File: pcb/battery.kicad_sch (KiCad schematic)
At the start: 38 parts

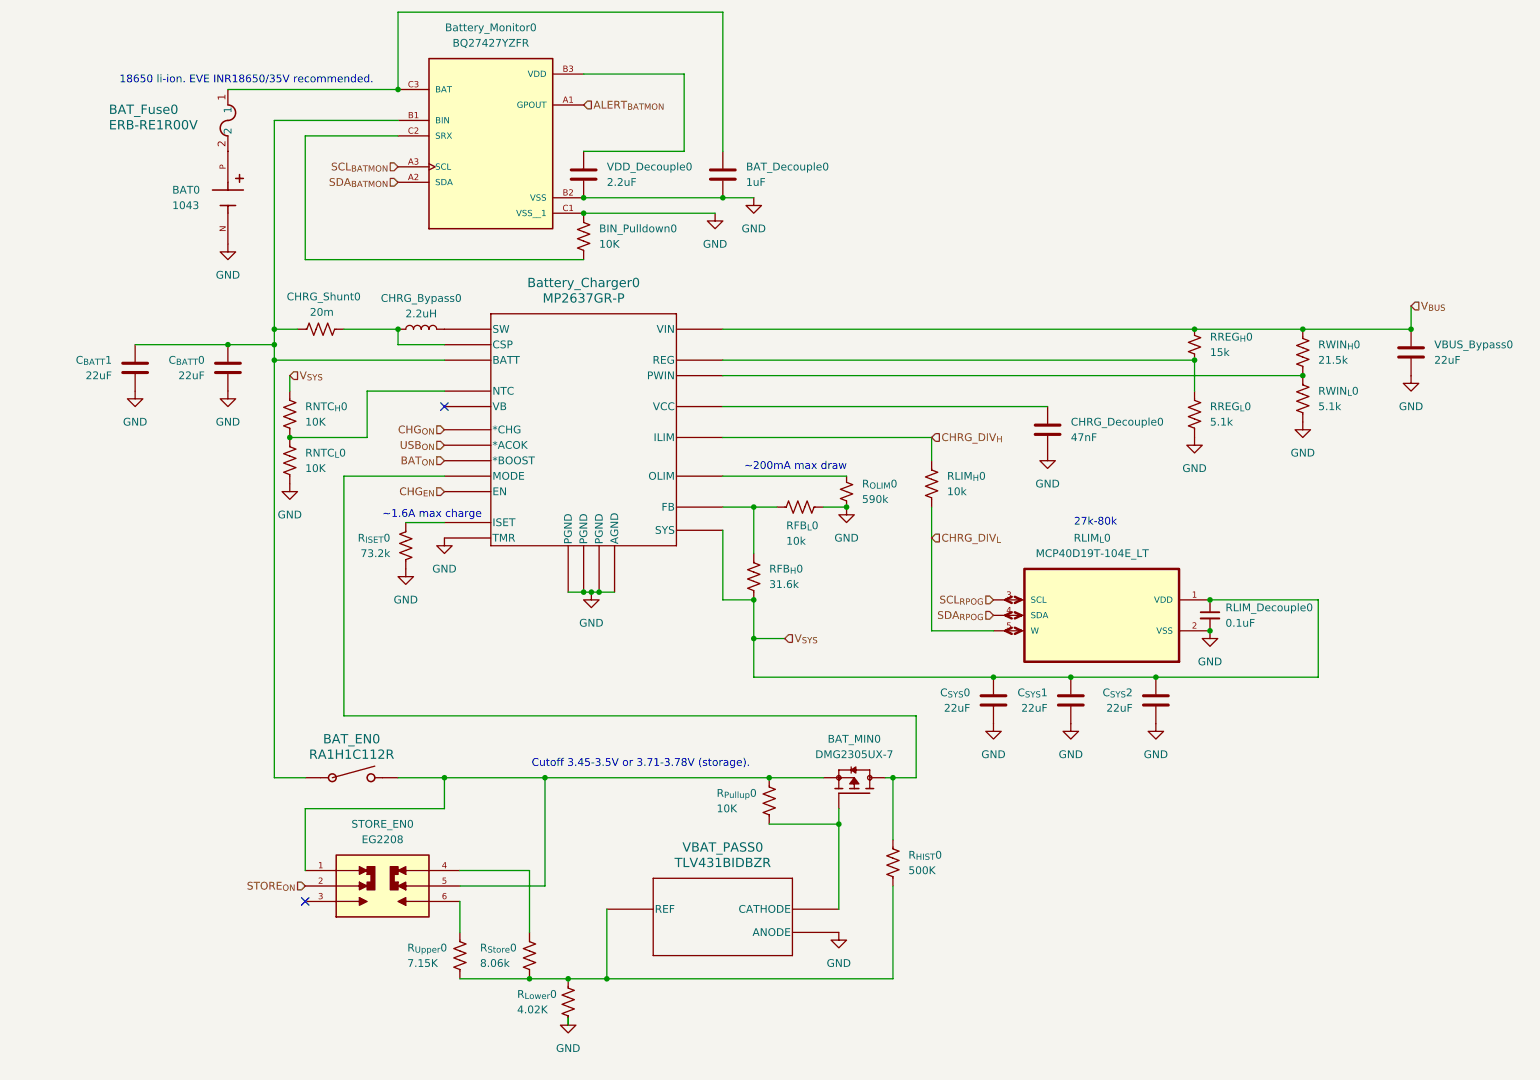
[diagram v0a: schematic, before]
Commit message: Label parts for JLCPCB
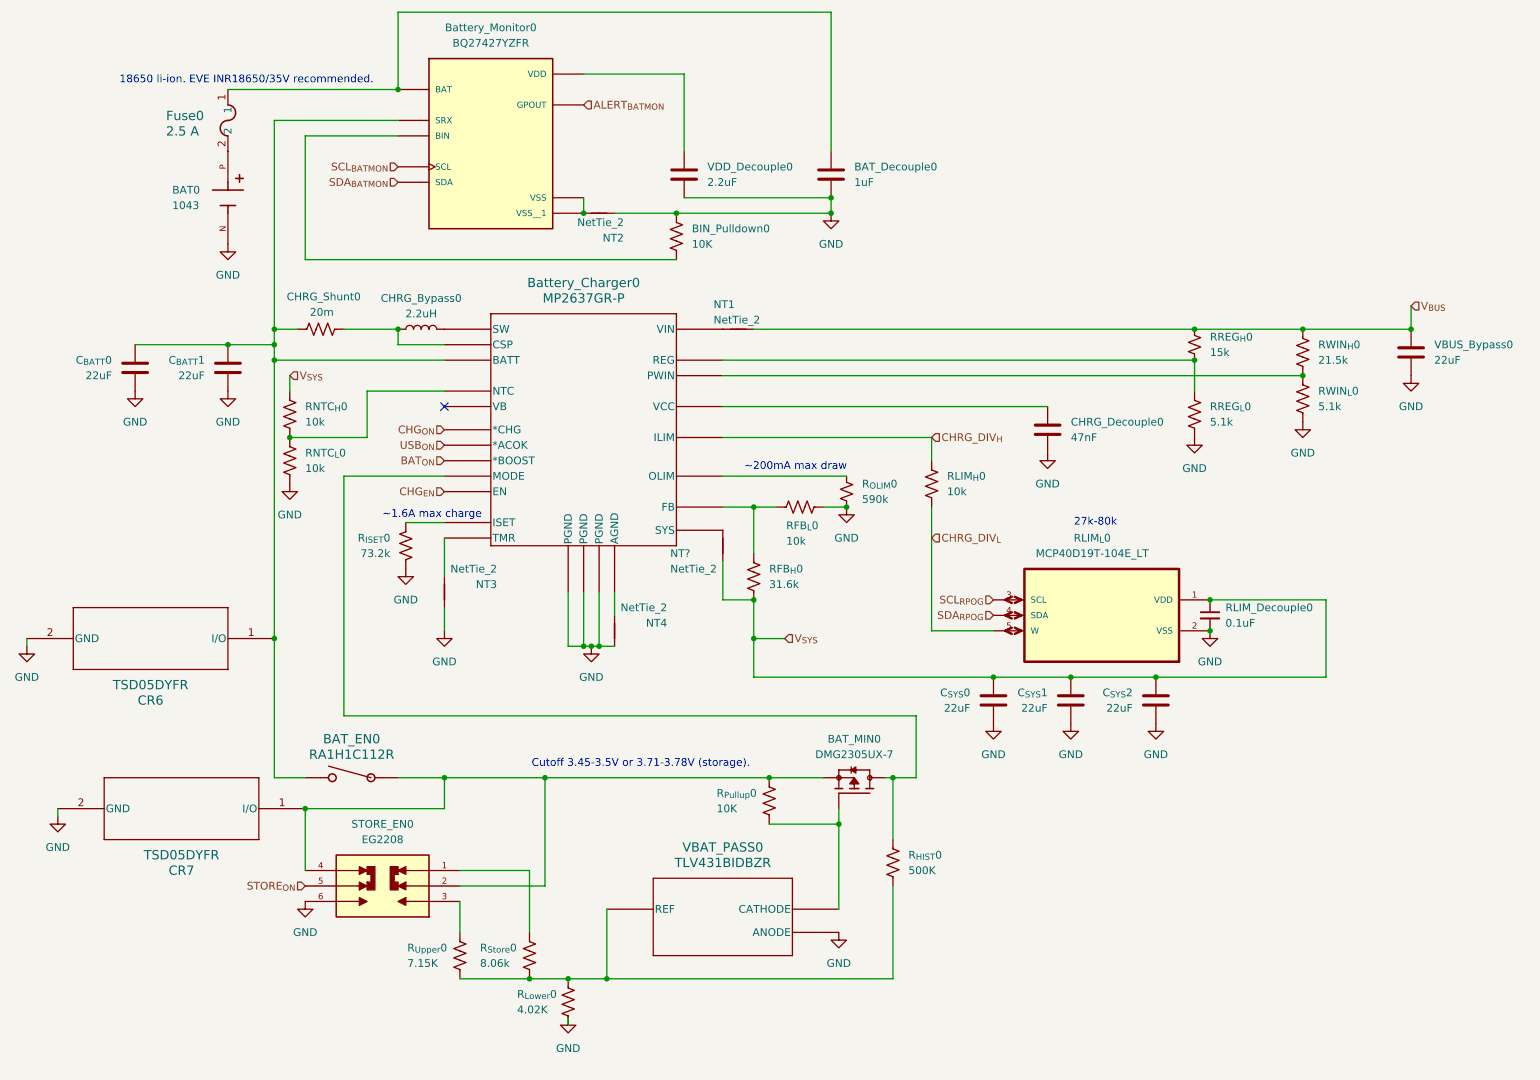
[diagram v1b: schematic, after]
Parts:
- added CR6, CR7: TSD05DYFR, TVS_SOD2_DYF_TEX, symbol TSD05DYFR:TSD05DYFR
- added NT1, NT2, NT3, NT4, NT?: NetTie_2, NetTie:NetTie-2_SMD_Pad0.5mm, symbol Device:NetTie_2
- BAT0: footprint 1043:BAT_1043 -> BAT_1043; symbol 1043:1043 -> 1042:1042; MAXIMUM_PACKAGE_HEIGHT 14.86mm -> 15.11mm; PARTREV J -> E; SNAPEDA_PN 1043 -> 1042
- BAT_MIN0: LCSC (none) -> C150470
- Battery_Charger0: LCSC (none) -> C97258
- Battery_Monitor0: footprint BQ27427YZFR:IC_BQ27427YZFR -> IC_BQ27427YZFR; LCSC (none) -> C6075475
- Fuse0: renamed from BAT_Fuse0; value ERB-RE1R00V -> 2.5 A; LCSC (none) -> C3166421
- RLIM_{L}0: LCSC (none) -> C623424
- RNTC_{H}0, RNTC_{L}0: value 10K -> 10k
- VBAT_PASS0: LCSC (none) -> C398375
- renumbered C_{BATT}1 to C_{BATT}0, C_{BATT}0 to C_{BATT}1
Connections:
- net GND: now also STORE_EN0.6, CR6.2 (GND), CR7.2 (GND), NT2.1, NT3.2, NT4.2; no longer Battery_Charger0.13 (TMR), Battery_Charger0.6 (AGND), Battery_Monitor0.B2 (VSS), Battery_Monitor0.C1 (VSS__1)
- net STORE_{ON}: now also STORE_EN0.5; no longer STORE_EN0.2
- net V_{BUS}: now also NT1.2; no longer Battery_Charger0.20 (VIN)
- net V_{SYS}: now also NT?.1; no longer Battery_Charger0.21 (SYS)
- net at Battery_Charger0.5 (BATT), CHRG_Shunt0.1, C_{BATT}0.1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: now also BAT_EN0.2, Battery_Monitor0.C2 (SRX), CR6.1 (I/O); no longer BAT_EN0.1, Battery_Monitor0.B1 (BIN)
- net at BIN_Pulldown0.2: now also Battery_Monitor0.B1 (BIN); no longer Battery_Monitor0.C2 (SRX)
- net at R_{Upper}0.1: now also STORE_EN0.3; no longer STORE_EN0.6
- net at STORE_EN0.4: now also BAT_EN0.1, BAT_MIN0.2, R_{Pullup}0.1, STORE_EN0.2, CR7.1 (I/O); no longer R_{Store}0.1
- new net: Battery_Monitor0.B2 (VSS), Battery_Monitor0.C1 (VSS__1), NT2.2
- new net: Battery_Charger0.21 (SYS), NT?.2
- new net: Battery_Charger0.13 (TMR), NT3.1
- new net: Battery_Charger0.20 (VIN), NT1.1
- new net: Battery_Charger0.6 (AGND), NT4.1
- new net: R_{Store}0.1, STORE_EN0.1
- no-connect marks 2 -> 1
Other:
- moved on the sheet: BAT_Decouple0, BIN_Pulldown0, VDD_Decouple0

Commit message: Add DNP for right hand
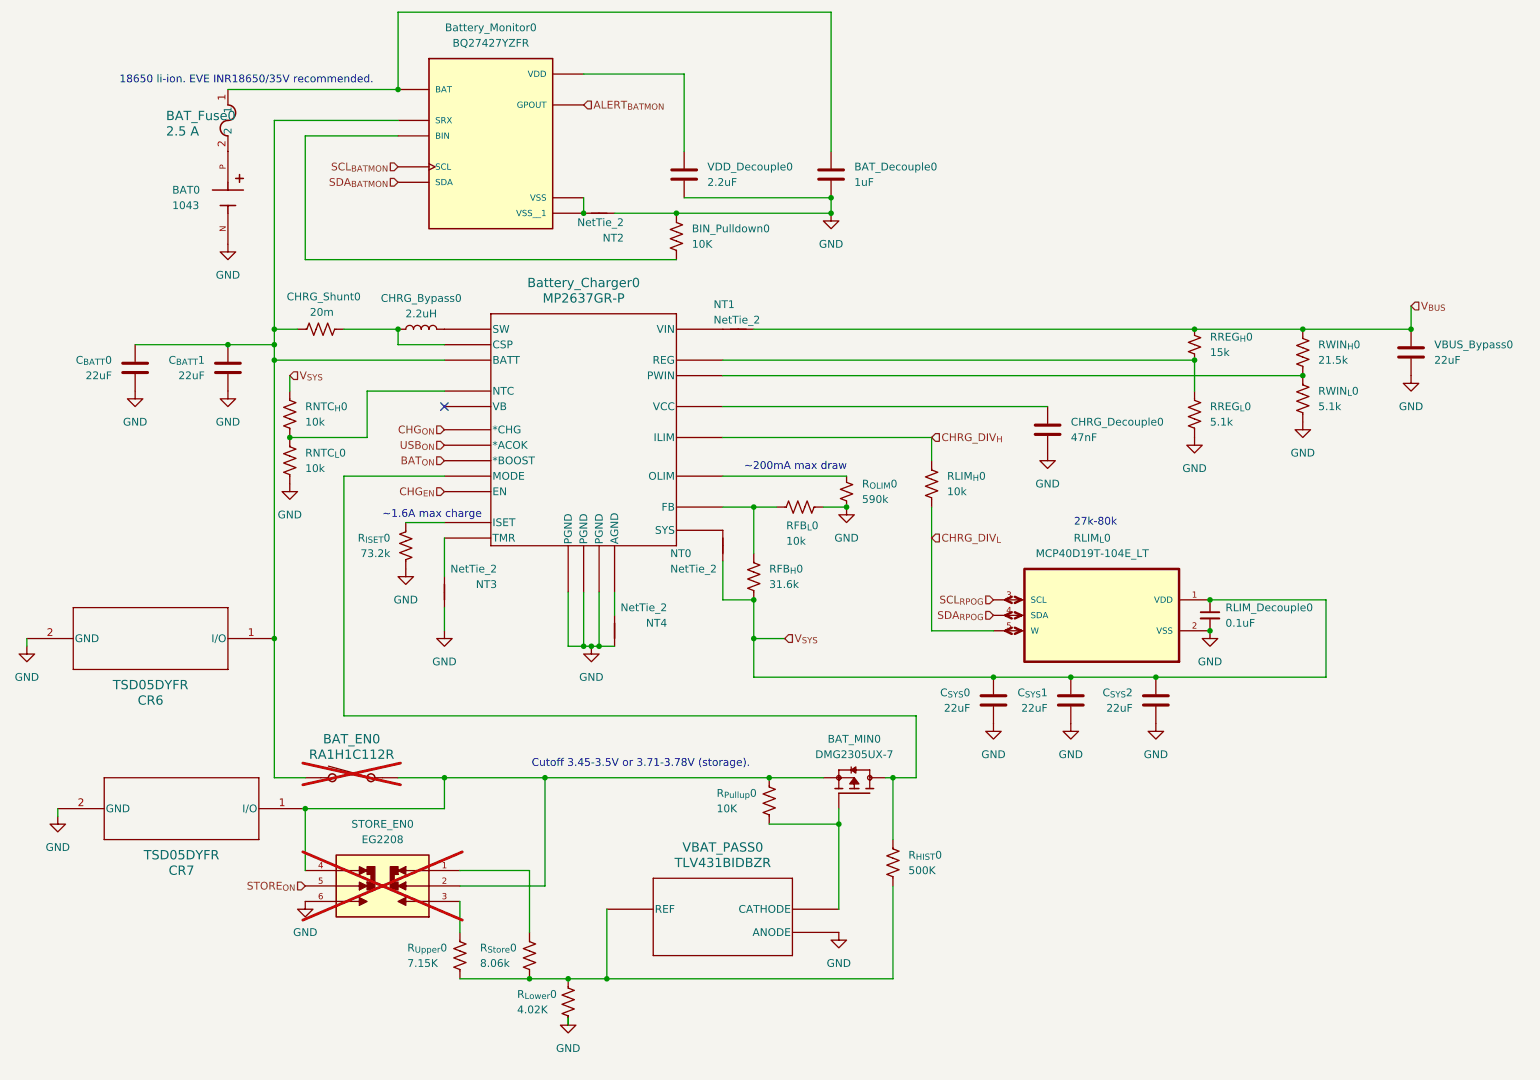
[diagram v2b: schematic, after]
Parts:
- BAT_EN0, STORE_EN0: now not fitted
- gave numbers to parts that had none: 1
- renumbered Fuse0 to BAT_Fuse0
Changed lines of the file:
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@@
 		(dnp no)
 		(fields_autoplaced yes)
-		(property "Reference" "#PWR030"
+		(property "Reference" "#PWR012"
 			(at 181.61 147.32 0)
 			(effects
@@
 		(dnp no)
 		(fields_autoplaced yes)
-		(property "Reference" "#PWR021"
+		(property "Reference" "#PWR04"
 			(at 85.09 121.92 0)
 			(effects
@@
 		(dnp no)
 		(fields_autoplaced yes)
-		(property "Reference" "#PWR013"
+		(property "Reference" "#PWR011"
 			(at 157.48 111.76 0)
 			(effects
@@
 		(dnp no)
 		(fields_autoplaced yes)
-		(property "Reference" "#PWR024"
+		(property "Reference" "#PWR018"
 			(at 232.41 97.79 0)
 			(effects
@@
 		(in_bom yes)
 		(on_board yes)
-		(dnp no)
+		(dnp yes)
 		(property "Reference" "BAT_EN0"
 			(at 76.2 143.51 0)
@@
 		(dnp no)
 		(fields_autoplaced yes)
-		(property "Reference" "#PWR027"
+		(property "Reference" "#PWR00"
 			(at 40.64 92.71 0)
 			(effects
@@
 		(on_board yes)
 		(dnp no)
-		(property "Reference" "NT?"
+		(property "Reference" "NT0"
 			(at 128.524 113.03 90)
 			(effects
@@
 		(dnp no)
 		(fields_autoplaced yes)
-		(property "Reference" "#PWR018"
+		(property "Reference" "#PWR08"
 			(at 154.94 63.5 0)
 			(effects
@@
 		(dnp no)
 		(fields_autoplaced yes)
-		(property "Reference" "#PWR012"
+		(property "Reference" "#PWR016"
 			(at 214.63 100.33 0)
 			(effects
@@
 		(dnp no)
 		(fields_autoplaced yes)
-		(property "Reference" "#PWR023"
+		(property "Reference" "#PWR017"
 			(at 217.17 132.08 0)
 			(effects
@@
 		(on_board yes)
 		(dnp no)
-		(property "Reference" "#PWR025"
+		(property "Reference" "#PWR07"
 			(at 115.57 134.62 0)
 			(effects
@@
 		(dnp no)
 		(fields_autoplaced yes)
-		(property "Reference" "#PWR010"
+		(property "Reference" "#PWR013"
 			(at 190.5 102.87 0)
 			(effects
@@
 		(dnp no)
 		(fields_autoplaced yes)
-		(property "Reference" "#PWR031"
+		(property "Reference" "#PWR014"
 			(at 194.31 147.32 0)
 			(effects
@@
 		(dnp no)
 		(fields_autoplaced yes)
-		(property "Reference" "#PWR016"
+		(property "Reference" "#PWR01"
 			(at 55.88 68.58 0)
 			(effects
@@
 		(dnp no)
 		(fields_autoplaced yes)
-		(property "Reference" "#PWR019"
+		(property "Reference" "#PWR010"
 			(at 156.21 181.61 0)
 			(effects
@@
 		(dnp no)
 		(fields_autoplaced yes)
-		(property "Reference" "#PWR028"
+		(property "Reference" "#PWR015"
 			(at 208.28 147.32 0)
 			(effects
@@
 		(in_bom yes)
 		(on_board yes)
-		(dnp no)
+		(dnp yes)
 		(property "Reference" "STORE_EN0"
 			(at 81.28 157.48 0)
@@
 		(dnp no)
 		(fields_autoplaced yes)
-		(property "Reference" "#PWR029"
+		(property "Reference" "#PWR019"
 			(at 250.19 90.17 0)
 			(effects
@@
 		(dnp no)
 		(fields_autoplaced yes)
-		(property "Reference" "#PWR022"
+		(property "Reference" "#PWR02"
 			(at 55.88 92.71 0)
 			(effects
@@
 		(dnp no)
 		(fields_autoplaced yes)
-		(property "Reference" "#PWR026"
+		(property "Reference" "#PWR03"
 			(at 66.04 107.95 0)
 			(effects
@@
 		(dnp no)
 		(fields_autoplaced yes)
-		(property "Reference" "#PWR?"
+		(property "Reference" "#PWR029"
 			(at 68.58 176.53 0)
 			(effects
@@
 		(dnp no)
 		(fields_autoplaced yes)
-		(property "Reference" "#PWR09"
+		(property "Reference" "#PWR05"
 			(at 91.44 132.08 0)
 			(effects
@@
 		(on_board yes)
 		(dnp no)
-		(property "Reference" "Fuse0"
+		(property "Reference" "BAT_Fuse0"
 			(at 45.72 41.148 90)
 			(effects
@@
 		(dnp no)
 		(fields_autoplaced yes)
-		(property "Reference" "#PWR017"
+		(property "Reference" "#PWR06"
 			(at 111.76 195.58 0)
 			(effects

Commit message: Label LCSC
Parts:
- BAT_Decouple0: LCSC (none) -> C2823
- BIN_Pulldown0, R_{Pullup}0: LCSC (none) -> C17414
- CHRG_Bypass0: LCSC (none) -> C70960
- CHRG_Decouple0: LCSC (none) -> C53134
- CHRG_Shunt0: LCSC (none) -> C158163
- C_{BATT}0, C_{BATT}1, C_{SYS}0, C_{SYS}1, C_{SYS}2, VBUS_Bypass0: LCSC (none) -> C12891
- RFB_{H}0: value 31.6k -> 31.6K; LCSC (none) -> C17623
- RFB_{L}0, RLIM_{H}0, RNTC_{H}0, RNTC_{L}0: value 10k -> 10K; LCSC (none) -> C17414
- RLIM_Decouple0: LCSC (none) -> C28233
- RREG_{H}0: value 15k -> 15K; LCSC (none) -> C17475
- RREG_{L}0, RWIN_{L}0: value 5.1k -> 5.1K; LCSC (none) -> C27834
- RWIN_{H}0: value 21.5k -> 21.5K; LCSC (none) -> C17545
- R_{HIST}0: LCSC (none) -> C3097783
- R_{ISET}0: value 73.2k -> 73.2K; LCSC (none) -> C17814
- R_{Lower}0: LCSC (none) -> C17663
- R_{OLIM}0: value 590k -> 590K; LCSC (none) -> C17762
- R_{Store}0: value 8.06k -> 8.06K; LCSC (none) -> C19006
- R_{Upper}0: LCSC (none) -> C17806
- VDD_Decouple0: LCSC (none) -> C377773
